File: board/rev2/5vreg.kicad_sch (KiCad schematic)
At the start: 21 parts, among them U1 SiC951

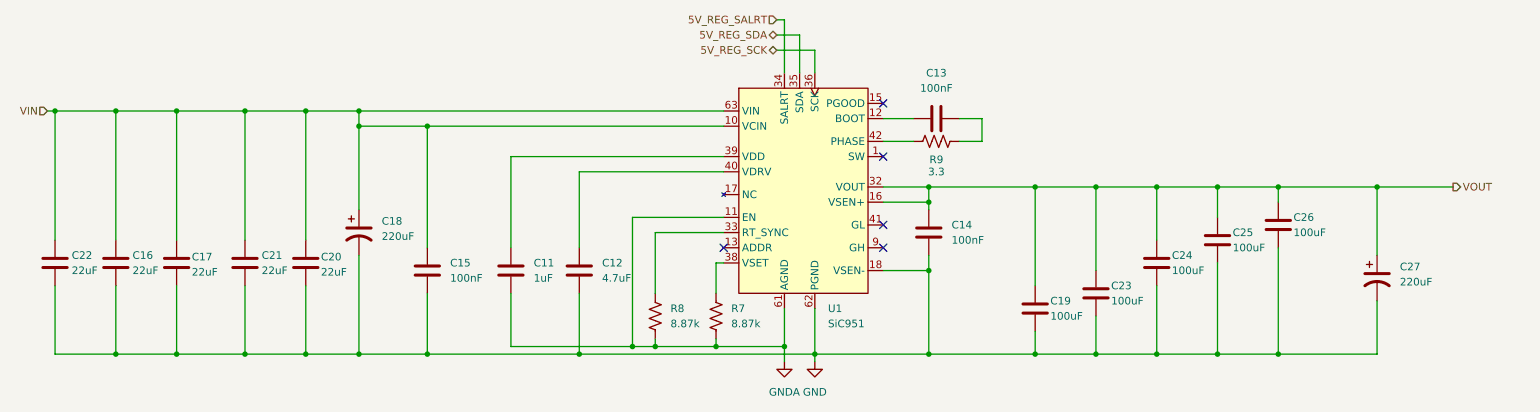
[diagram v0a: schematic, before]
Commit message: remove sic951 --> start doing sic451
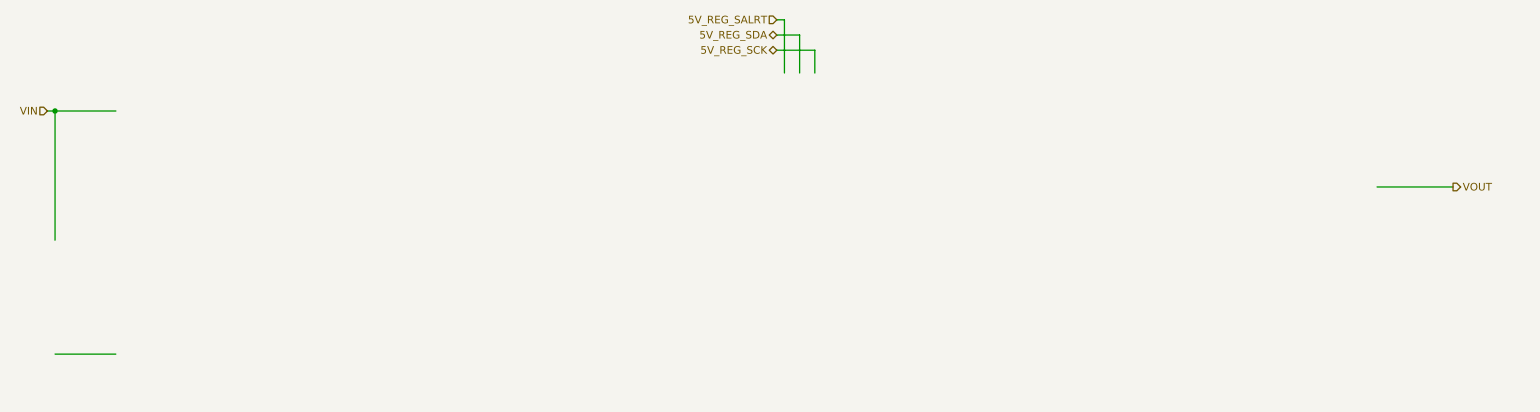
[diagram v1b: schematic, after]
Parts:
- removed C11: 1uF, symbol Device:C
- removed C12: 4.7uF, symbol Device:C
- removed C13, C14, C15: 100nF, symbol Device:C
- removed C16, C17, C20, C21, C22: 22uF, symbol Device:C
- removed C18, C27: 220uF, symbol Device:C_Polarized_US
- removed C19, C23, C24, C25, C26: 100uF, symbol Device:C
- removed R7, R8: 8.87k, symbol Device:R_US
- removed R9: 3.3, symbol Device:R_US
- removed U1: SiC951, Vishay_DCDC:MLP59-A6C, symbol Vishay_DCDC:SiC951
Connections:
- no-connect marks 5 -> 0

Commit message: Finish most of power section of rev2 PCB
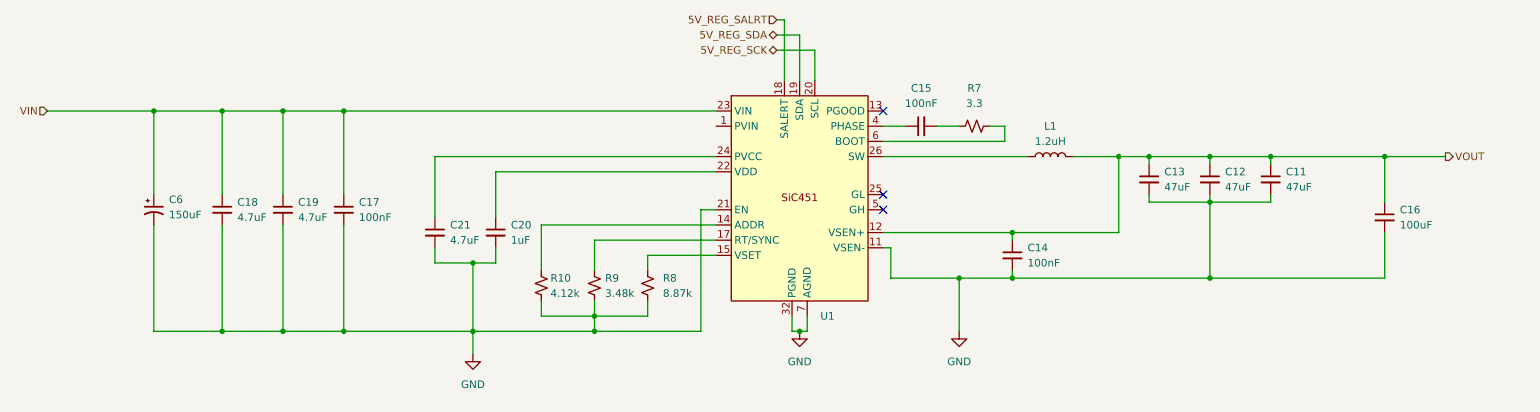
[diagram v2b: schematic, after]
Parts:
- added C11, C12, C13: 47uF, symbol Device:C_Small
- added C14, C15, C17: 100nF, symbol Device:C_Small
- added C16: 100uF, symbol Device:C_Small
- added C18, C19, C21: 4.7uF, symbol Device:C_Small
- added C20: 1uF, symbol Device:C_Small
- added C6: 150uF, symbol Device:C_Polarized_Small_US
- added L1: 1.2uH, symbol Device:L
- added R10: 4.12k, symbol Device:R_Small_US
- added R7: 3.3, symbol Device:R_Small_US
- added R8: 8.87k, symbol Device:R_Small_US
- added R9: 3.48k, symbol Device:R_Small_US
- added U1: ~, Vishay_DCDC:POWERPAK_MLP34-57_VIS, symbol Vishay_DCDC:SiC451ED-T1-GE3
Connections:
- net 5V_REG_SALRT: now also U1.18 (SALERT)
- net 5V_REG_SCK: now also U1.20 (SCL)
- net 5V_REG_SDA: now also U1.19 (SDA)
- net VIN: now also C17.1, C18.1, C19.1, C6.1, U1.23 (VIN)
- net VOUT: now also C11.1, C12.1, C13.1, C14.1, C16.1, L1.2, U1.12 (VSEN+)
- new net: L1.1, U1.26 (SW)
- new net: C20.1, U1.22 (VDD)
- new net: R10.1, U1.14 (ADDR)
- new net: R8.1, U1.15 (VSET)
- new net: R9.1, U1.17 (RT/SYNC)
- new net: C21.1, U1.24 (PVCC)
- new net: C15.1, U1.4 (PHASE)
- new net: R7.2, U1.6 (BOOT)
- new net: C15.2, R7.1
- new net GND: C11.2, C12.2, C13.2, C14.2, C16.2, C17.2, C18.2, C19.2, C20.2, C21.2, C6.2, R10.2, R8.2, R9.2, U1.11 (VSEN-), U1.21 (EN), U1.32 (PGND), U1.7 (AGND)
- no-connect marks 0 -> 3

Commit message: More board stuff
(better clk routing, etc.)
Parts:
- added C23, C27: 47uF, symbol Device:C_Small
- C11, C12, C13: ESR (none) -> 2m
- L1: value 1.2uH -> 820nH; Part (none) -> TMPC1265HP-R82MG-D
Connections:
- net GND: now also C23.2, C27.2
- net VOUT: now also C23.1, C27.1
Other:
- moved on the sheet: C16, L1
